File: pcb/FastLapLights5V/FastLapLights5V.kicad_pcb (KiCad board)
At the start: 4 copper layers, 27.3 x 40 mm, 29 parts, among them IC1 74HCT1G125GV,125, J1 POWER_CON, J2 SWD, J3 I2C, J4 IO, U1 STM32C011F4Px, U2 AP63205WU, U3 AP2112K-3.3, U4 BD33FC0FP

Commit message: change jlcpcb parts
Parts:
- removed the C12 at (57.0, 107.3)
- removed C13: 22uF, Capacitor_SMD:C_0603_1608Metric
- removed the C7 at (48.6, 108.4)
- removed the C8 at (54.8, 110.0)
- removed U4: BD33FC0FP, Package_TO_SOT_SMD:TO-252-2
- added C10: 4.7uF, Capacitor_SMD:C_0603_1608Metric, F.Cu at (48.6, 108.4)
- added C11: 4.7uF, Capacitor_SMD:C_0603_1608Metric, F.Cu at (54.8, 110.0)
- C3: value 100uF -> 220uF; footprint Library:CP_Elec_A768KS227M1VLAE024 -> Library:CP_220_Honor_Elec_HV1E227M0810PZ
- C5: value 100nF -> 0.1uF; footprint Capacitor_SMD:C_0805_2012Metric -> Capacitor_SMD:C_0603_1608Metric
- C6: footprint Capacitor_SMD:C_0805_2012Metric -> Capacitor_SMD:C_0603_1608Metric
- C7: renamed from C9; footprint Capacitor_SMD:C_0805_2012Metric -> Capacitor_SMD:C_0603_1608Metric
- L1: value 22.8uH -> 22uH; footprint Library:L_EATON_DR1030-220-R -> Library:L_Chilisin_Elec_BPSC00101140220M00
- moved C4 9.95 mm to (52.0, 91.0), turned to -90 degrees
- moved C5 9.18 mm to (62.4, 89.8), turned to 90 degrees
- moved J2 9.00 mm to (60.9, 108.9), turned to 0 degrees
- moved J3 8.06 mm to (63.5, 117.6), turned to -90 degrees
- moved C6 5.60 mm to (54.2, 90.8), turned to -90 degrees
- moved U2 5.51 mm to (58.8, 90.0), turned to 0 degrees
- moved L1 4.81 mm to (61.5, 99.3)
- moved C9 4.09 mm to (58.1, 106.9), turned to -90 degrees
- moved C7 3.98 mm to (53.8, 96.3), turned to -90 degrees
- moved C8 3.25 mm to (56.4, 106.9), turned to -90 degrees
- moved R1 1.79 mm to (66.0, 124.1)
- moved C2 1.00 mm to (57.2, 116.3)
- moved J4 0.92 mm to (44.9, 115.7)
- moved C1 0.90 mm to (57.2, 114.7)
- moved JP1 0.82 mm to (61.9, 124.1)
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- renumbered C14 to C12, C10 to C8, C11 to C9
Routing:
- net +3.3V: track 32.8 -> 53.2 mm, vias 1 -> 2
- net /VRAIL_CAP: track 44.9 -> 31.1 mm, vias 2 -> 0
- net /SWD_SWCLK: track 12.3 -> 23.1 mm
- net /SWD_SWDIO: track 11.0 -> 19.5 mm
- net /SWD_NRST: track 11.4 -> 19.9 mm, vias 0 -> 1
- net Net-(U2-SW): track 14.4 -> 7.20 mm
- net /I2C_SCL: track 10.8 -> 5.78 mm, vias 1 -> 0
- net GND: track 12.9 -> 16.5 mm, vias 40 -> 23
- net /I2C_SDA: track 12.9 -> 9.39 mm, vias 1 -> 0
- net +5V: track 67.5 -> 68.7 mm
- net /START_LIGHTS_5V: track 6.22 -> 5.05 mm
- net /TRACK_LIGHTS_R: track 10.2 -> 11.2 mm, vias 0 -> 1
- net /IO_POWER_RAIL_DATA: track 25.2 -> 24.3 mm
- net Net-(JP1-A): track 3.19 -> 4.01 mm
- net /IO_POWER_RAIL_INT: track 11.3 -> 10.7 mm
- added copper zone on F.Cu, net +5V
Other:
- board size 27.3 x 40 mm -> 25 x 39.2 mm
- board text added: "."

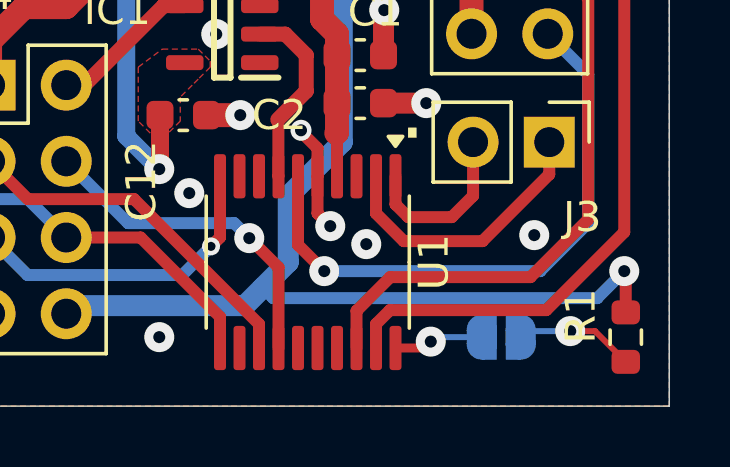
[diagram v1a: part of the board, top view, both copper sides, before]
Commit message: change sj start light - pit lane light
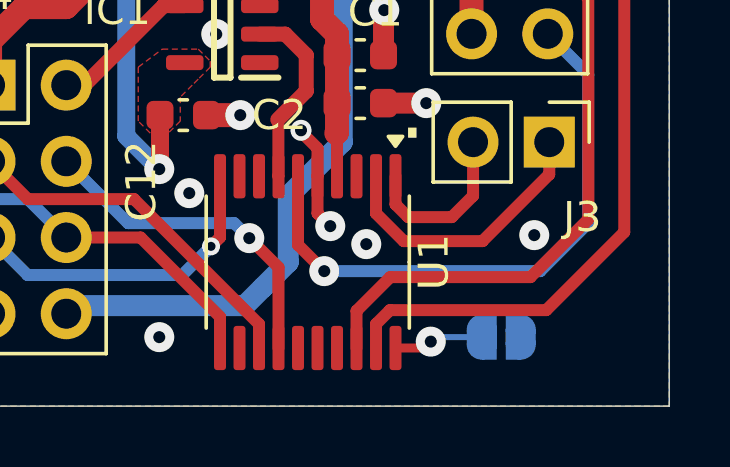
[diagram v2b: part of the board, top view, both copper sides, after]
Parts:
- removed R1: 4k7, Resistor_SMD:R_0603_1608Metric
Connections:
- JP1 pad 1: Net-(JP1-A) -> GND
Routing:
- net +3.3V: track 53.2 -> 39.2 mm, vias 2 -> 1
- net Net-(JP1-A): track 4.01 -> 0.00 mm, vias 1 -> 0

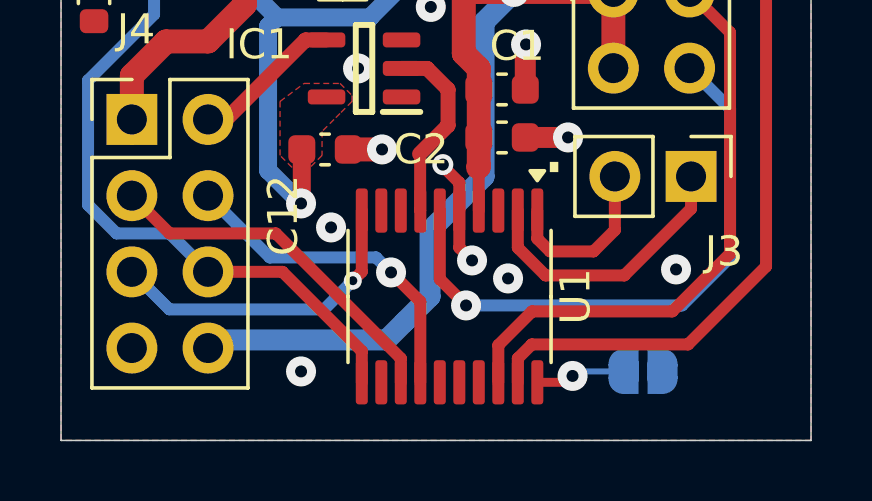
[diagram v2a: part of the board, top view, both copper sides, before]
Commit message: fix issues with decoding manchester data and make it more reliable
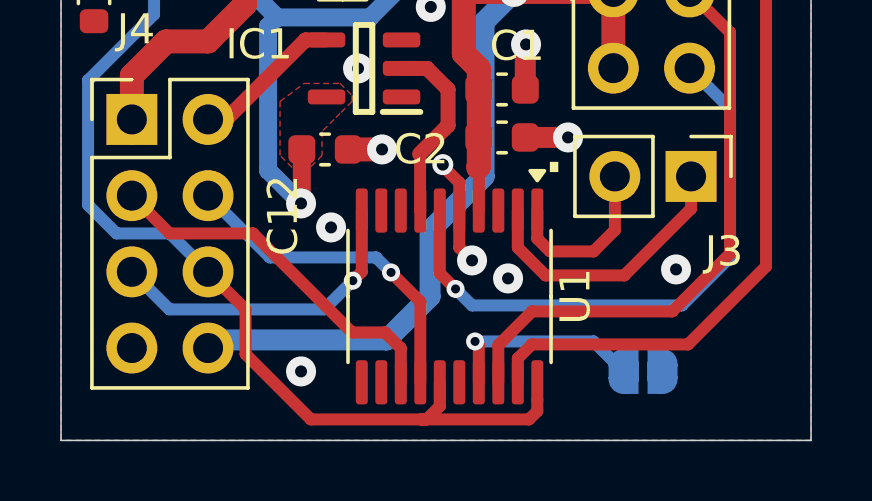
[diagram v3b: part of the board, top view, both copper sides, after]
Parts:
- turned JP1 to 0 degrees
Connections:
- JP1 pad 1: GND -> /SJ1
- JP1 pad 2: Net-(JP1-B) -> GND
- U1 pad 11: /IO_POWER_RAIL_DATA -> unconnected-(U1-PA4-Pad11)
- U1 pad 15: unconnected-(U1-PA8-Pad15) -> /IO_POWER_RAIL_DATA
- U1 pad 17: unconnected-(U1-PA10/PA12-Pad17) -> /SJ1
- U1 pad 20: Net-(JP1-B) -> /IO_POWER_RAIL_DATA
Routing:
- net /IO_POWER_RAIL_DATA: track 24.3 -> 33.1 mm
- net /SJ1: track 0.00 -> 6.78 mm, vias 0 -> 1
- net Net-(JP1-B): track 3.03 -> 0.00 mm, vias 1 -> 0

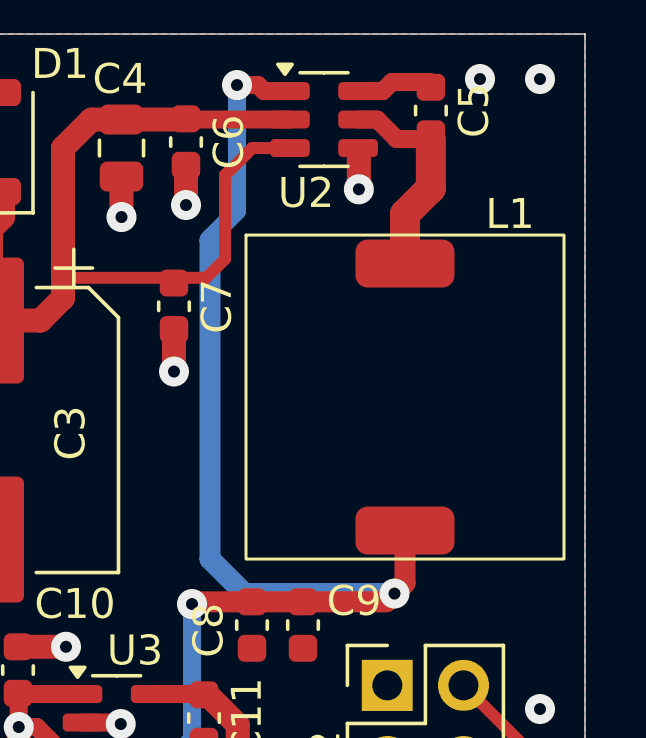
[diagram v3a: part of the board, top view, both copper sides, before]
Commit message: activate solder jumper pin, replace sold-out components
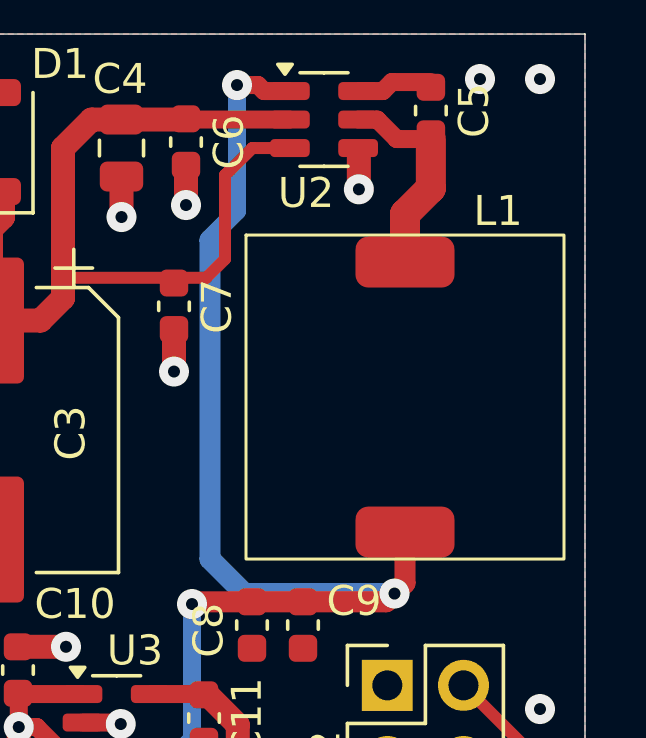
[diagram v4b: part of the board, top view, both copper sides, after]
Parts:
- L1: footprint Library:L_Chilisin_Elec_BPSC00101140220M00 -> Library:L_SXN_SMDRH104R-220MT
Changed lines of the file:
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@@
 		)
 	)
-	(footprint "Library:L_Chilisin_Elec_BPSC00101140220M00"
+	(footprint "Library:L_SXN_SMDRH104R-220MT"
 		(layer "F.Cu")
 		(at 61.5 99.3)
@@
 		(tags "SMD Shielded Power Inductors - BPSC Series")
 		(property "Reference" "L1"
-			(at 3.5 -6.1 0)
+			(at 3.1 -6.2 0)
 			(layer "F.SilkS")
 			(effects
@@
 			(at 0 6.6 0)
 			(layer "F.Fab")
-			(hide yes)
-			(effects
-				(font
-					(size 1 1)
-					(thickness 0.15)
-				)
-			)
-		)
-		(property "Footprint" "Library:L_Chilisin_Elec_BPSC00101140220M00"
-			(at 0 0 0)
-			(unlocked yes)
-			(layer "F.Fab")
-			(hide yes)
-			(effects
-				(font
-					(size 1.27 1.27)
-					(thickness 0.15)
-				)
-			)
-		)
-		(property "Datasheet" "https://www.lcsc.com/datasheet/lcsc_datasheet_2410121503_Chilisin-Elec-BPSC00101140220M00_C5201662.pdf"
+			(effects
+				(font
+					(size 1 1)
+					(thickness 0.15)
+				)
+			)
+		)
+		(property "Footprint" "Library:L_SXN_SMDRH104R-220MT"
+			(at 0 0 0)
+			(unlocked yes)
+			(layer "F.Fab")
+			(hide yes)
+			(effects
+				(font
+					(size 1.27 1.27)
+					(thickness 0.15)
+				)
+			)
+		)
+		(property "Datasheet" ""
 			(at 0 8.2 0)
 			(unlocked yes)
@@
 			)
 		)
-		(property "LCSC" "C5201662"
+		(property "LCSC" "C72414"
 			(at 0 0 0)
 			(unlocked yes)
@@
 		)
 		(pad "1" smd roundrect
-			(at 0 -4.45)
-			(size 3.3 1.6)
+			(at 0 -4.5)
+			(size 3.3 1.7)
 			(layers "F.Cu" "F.Paste" "F.Mask")
 			(roundrect_rratio 0.25)
@@
 		)
 		(pad "2" smd roundrect
-			(at 0 4.45)
-			(size 3.3 1.6)
+			(at 0 4.5)
+			(size 3.3 1.7)
 			(layers "F.Cu" "F.Paste" "F.Mask")
 			(roundrect_rratio 0.25)
@@
 		(tags "solder jumper open")
 		(property "Reference" "JP1"
-			(at 0 -2 360)
+			(at 0 -2 0)
 			(layer "B.SilkS")
 			(effects
@@
 		)
 		(property "Value" "SP"
-			(at 0 -1.9 360)
+			(at 0 -1.9 0)
 			(layer "B.Fab")
 			(hide yes)

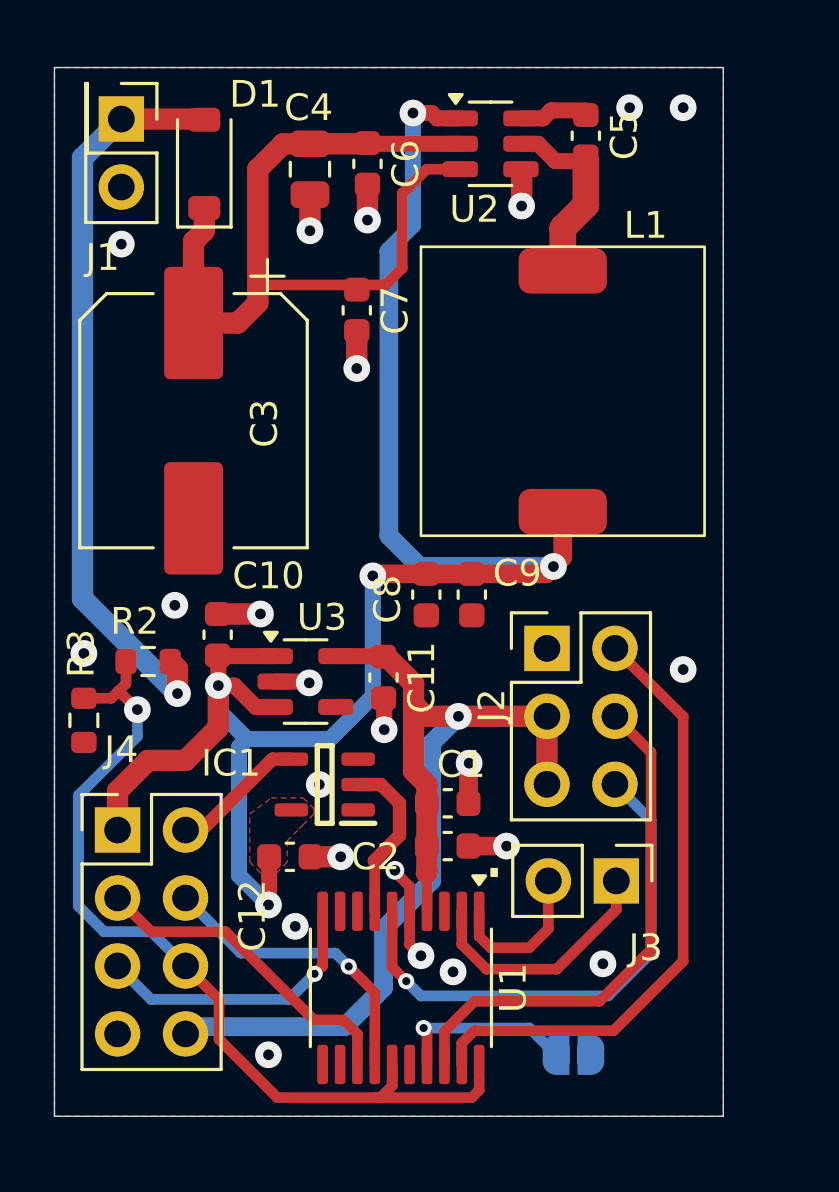
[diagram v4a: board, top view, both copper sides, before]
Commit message: - add race mode practice session - i2c to uart for faster datastreaming to displays - fix timer issue with tim1
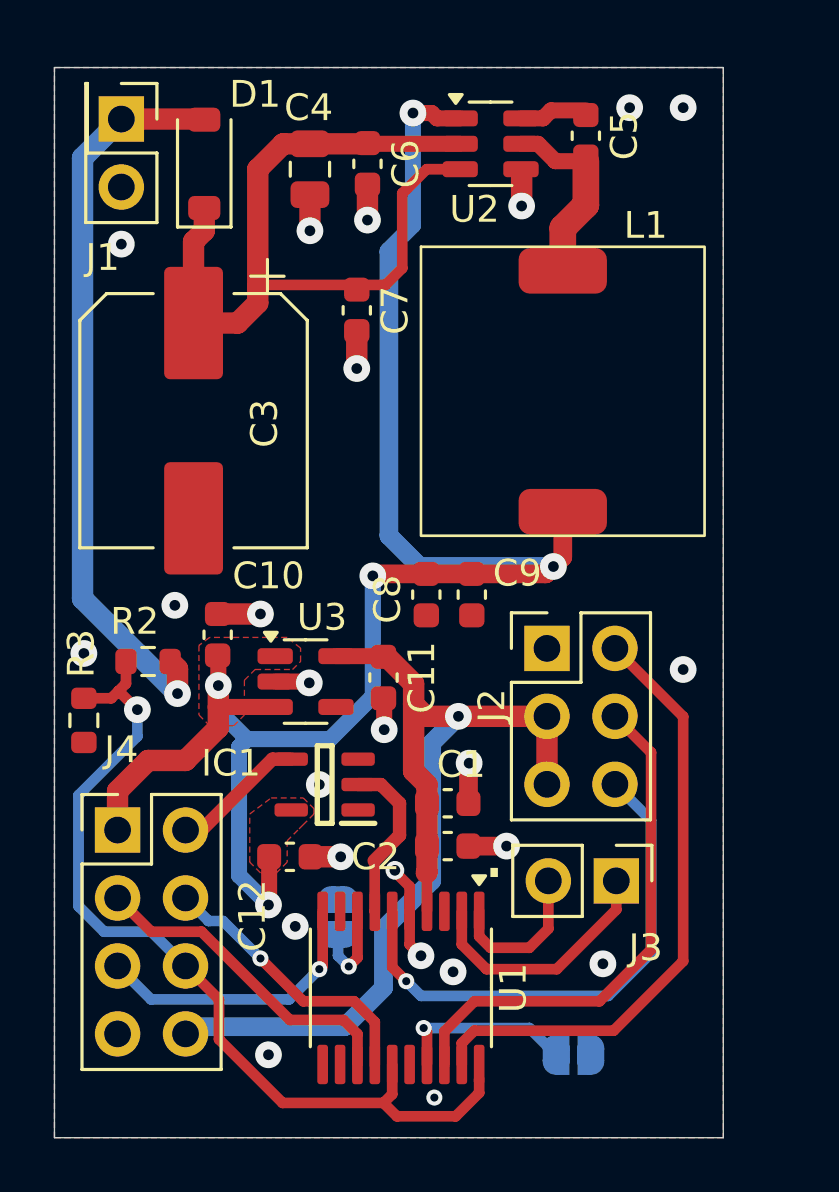
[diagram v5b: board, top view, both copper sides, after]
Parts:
- added JP2: SP, Jumper:SolderJumper-2_P1.3mm_Open_RoundedPad1.0x1.5mm, B.Cu at (53.1, 119.0)
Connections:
- net /I2C_SCL renamed /UART_RX
- net /I2C_SDA renamed /UART_TX
- net /IO_POWER_RAIL_INT renamed /SW_RACE_MODE
- net /SJ1 renamed /SJ1_1
- U1 pad 8: unconnected-(U1-PA1-Pad8) -> /SJ2_1
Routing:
- net /SJ2_1: track 0.00 -> 3.56 mm, vias 0 -> 1
- net +5V: track 68.7 -> 66.2 mm
- net /TRACK_LIGHTS_R: track 11.2 -> 10.6 mm
- net /IO_POWER_RAIL_DATA: track 33.1 -> 33.7 mm
- net GND: vias 23 -> 24
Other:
- board size 25 x 39.2 mm -> 25 x 40 mm

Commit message: fix workaround
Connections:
- U1 pad 20: /IO_POWER_RAIL_DATA -> unconnected-(U1-PB6-Pad20)
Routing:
- net /IO_POWER_RAIL_DATA: track 33.7 -> 29.0 mm
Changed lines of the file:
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@@
 	(title_block
 		(title "FastLapLights5V")
-		(date "2025-04-14")
-		(rev "MK6")
+		(date "2025-10-14")
+		(rev "MK7")
 	)
 	(layers
@@
 	(net 25 "Net-(U2-BST)")
 	(net 26 "unconnected-(U3-NC-Pad4)")
+	(net 27 "unconnected-(U1-PB6-Pad20)")
 	(footprint "Connector_PinHeader_2.54mm:PinHeader_2x04_P2.54mm_Vertical"
 		(layer "F.Cu")
@@
 			(layers "F.Cu" "F.Paste" "F.Mask")
 			(roundrect_rratio 0.25)
-			(net 11 "/IO_POWER_RAIL_DATA")
+			(net 27 "unconnected-(U1-PB6-Pad20)")
 			(pinfunction "PB6")
-			(pintype "bidirectional")
+			(pintype "bidirectional+no_connect")
 		)
 		(model "${KICAD8_3DMODEL_DIR}/Package_SO.3dshapes/TSSOP-20_4.4x6.5mm_P0.65mm.wrl"
@@
 	)
 	(segment
-		(start 57.5 126.4)
-		(end 58.375 125.525)
-		(width 0.4)
-		(layer "F.Cu")
-		(net 11)
-	)
-	(segment
-		(start 55.3 126.4)
-		(end 57.5 126.4)
-		(width 0.4)
-		(layer "F.Cu")
-		(net 11)
-	)
-	(segment
 		(start 44.9 110.5)
 		(end 45.6 111.2)
@@
 		(width 0.4)
 		(layer "F.Cu")
-		(net 11)
-	)
-	(segment
-		(start 54.8 125.9)
-		(end 55.3 126.4)
-		(width 0.4)
-		(layer "F.Cu")
-		(net 11)
-	)
-	(segment
-		(start 58.375 125.525)
-		(end 58.375 125.0125)
-		(width 0.4)
-		(layer "F.Cu")
